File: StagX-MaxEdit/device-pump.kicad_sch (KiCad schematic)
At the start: 0 parts

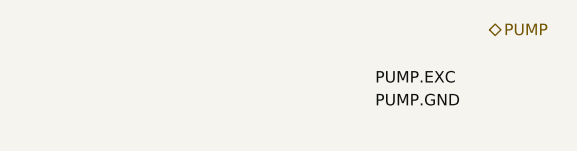
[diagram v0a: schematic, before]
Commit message: Added initial version for loom routing
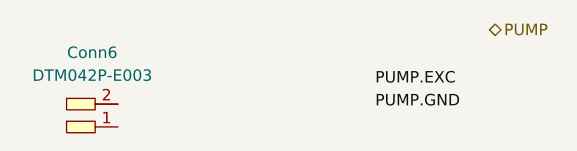
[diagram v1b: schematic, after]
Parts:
- added Conn6: Deutsch_DTM_2P_Pin, symbol Connectors_SUFST:Deutsch_DTM_2P_Pin
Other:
- title: (none) -> DEVICE - PUMP
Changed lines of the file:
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@@
 (kicad_sch (version 20230121) (generator eeschema)
   (paper "A4")
+  (title_block
+    (title "DEVICE - PUMP")
+  )
   (label "PUMP.GND" (at 162.56 85.09 0) (fields_autoplaced)
     (effects (font (size 1.27 1.27)) (justify left bottom))
@@
     (effects (font (size 1.27 1.27)) (justify left))
   )
+  (symbol (lib_id "Connectors_SUFST:Deutsch_DTM_2P_Pin") (at 132.08 80.01 0) (unit 1)
+    (in_bom yes) (on_board yes) (dnp no) (fields_autoplaced)
+    (property "Reference" "Conn6" (at 131.1275 78.74 0)
+      (effects (font (size 1.27 1.27)))
+    )
+    (property "Value" "Deutsch_DTM_2P_Pin" (at 132.08 80.01 0)
+      (effects (font (size 1.27 1.27)) hide)
+    )
+    (property "Footprint" "" (at 132.08 81.915 0)
+      (effects (font (size 1.27 1.27)) hide)
+    )
+    (property "Datasheet" "" (at 132.08 81.915 0)
+      (effects (font (size 1.27 1.27)) hide)
+    )
+    (property "P/N" "DTM042P-E003" (at 131.1275 81.28 0)
+      (effects (font (size 1.27 1.27)))
+    )
+    (pin "2")
+    (pin "1")
+    (instances
+      (project "StagX"
+        (path "/03011643-0690-4b85-ab78-d6a62dae52b1/51825ed1-c28d-47fe-be22-df39d19065ff"
+          (reference "Conn6") (unit 1)
+        )
+        (path "/03011643-0690-4b85-ab78-d6a62dae52b1/2cf8afa7-2cb2-4c65-9a6a-3a43fa257b78"
+          (reference "Conn7") (unit 1)
+        )
+      )
+    )
+  )
 )
